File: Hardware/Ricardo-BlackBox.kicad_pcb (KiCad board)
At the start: 4 copper layers, 45.1 x 35.1 mm, 83 parts, among them J1 RBUS, J2 USB_C_Receptacle_USB2.0, J3 Conn_01x08_Pin, U1 ESP32-S3, U2 SN65HVD230, U3 LM66200DRLR, U4 MAX77827AEFD+T, U5 SC4215ASTRT, U7 LM66200DRLR, Y1 R940000171

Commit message: Rearranging ESP32 CLC
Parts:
- moved C5 2.61 mm to (94.6, 60.0), turned to 180 degrees
- moved C1 2.51 mm to (94.6, 59.0), turned to 180 degrees
- moved L1 2.35 mm to (96.6, 59.0), turned to 0 degrees
- moved C4 1.99 mm to (96.6, 60.0), turned to 0 degrees
- moved C6 1.67 mm to (98.1, 59.5), turned to 90 degrees
- moved C7 1.30 mm to (99.1, 57.5)
- moved C9 1.30 mm to (100.1, 57.5)
- moved C11 0.20 mm to (108.8, 57.9)
- moved R6 0.15 mm to (106.9, 57.9)
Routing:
- net +3V3: track 25.6 -> 22.1 mm
- net /CAN_RX: track 30.5 -> 31.5 mm
- net /CHIP_PU: track 29.8 -> 28.8 mm
- net /CAN_TX: track 25.9 -> 26.9 mm
- net /BOOT: track 34.6 -> 33.7 mm
- net Net-(C6-Pad1): track 4.07 -> 4.67 mm
- net GND: vias 53 -> 54
- added copper zone on F.Cu, net Net-(C6-Pad1)

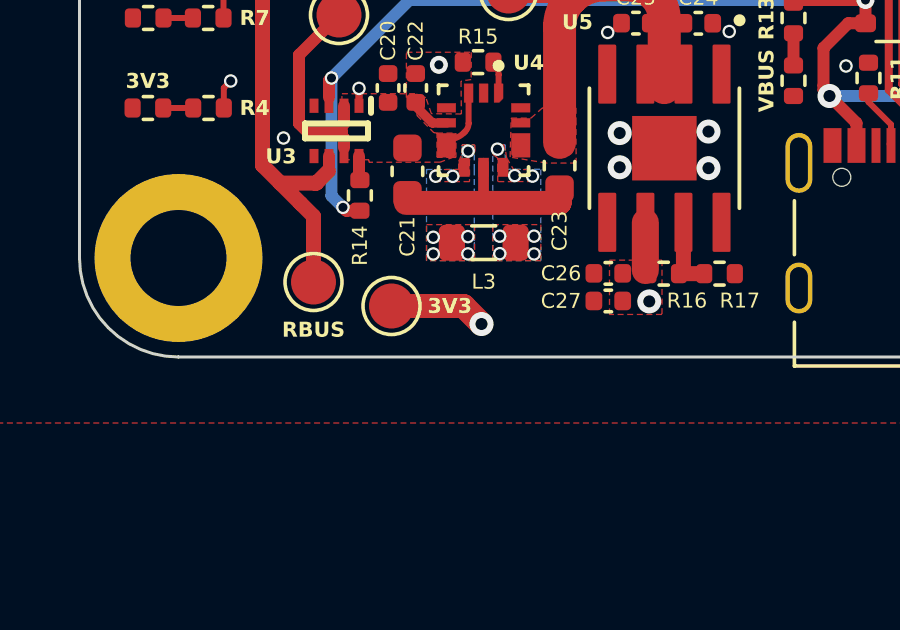
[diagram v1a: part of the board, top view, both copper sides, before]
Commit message: Fixed fill zones
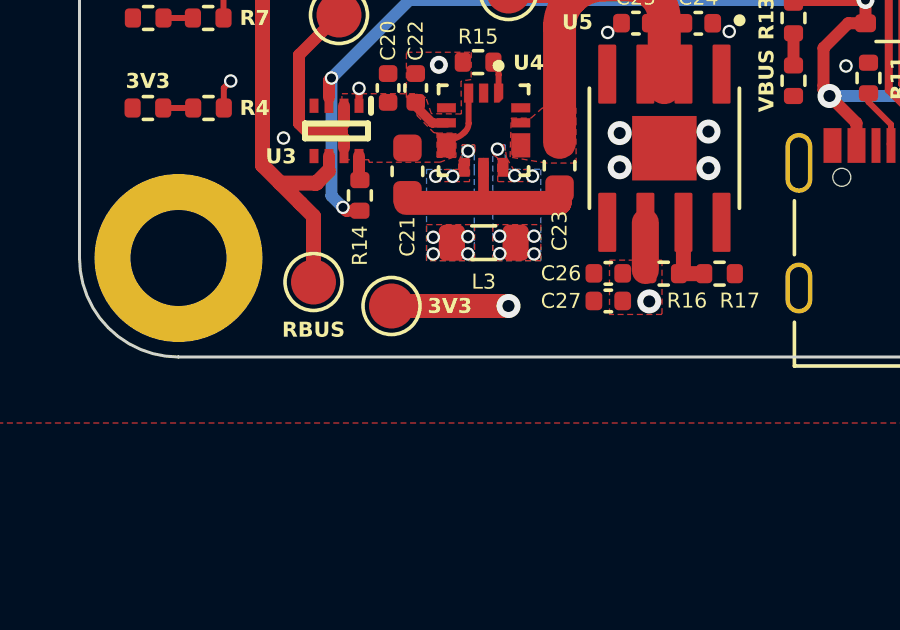
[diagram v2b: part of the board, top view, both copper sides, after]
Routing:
- net +3V3: track 22.1 -> 22.7 mm
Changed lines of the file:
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@@
 	)
 	(segment
-		(start 91.925 79.19)
-		(end 89.525 79.19)
-		(width 0.8)
-		(layer "F.Cu")
-		(net 2)
-	)
-	(segment
 		(start 113.275 70.512)
 		(end 113.275 70.94)
@@
 	)
 	(segment
-		(start 92.525 79.79)
-		(end 91.925 79.19)
+		(start 93.425 79.19)
+		(end 89.525 79.19)
 		(width 0.8)
 		(layer "F.Cu")
@@
 	)
 	(via
-		(at 92.525 79.79)
+		(at 93.425 79.19)
 		(size 0.8)
 		(drill 0.4)
@@
 	)
 	(zone
-		(net 3)
-		(net_name "VBUS")
-		(layer "F.Cu")
-		(name "$teardrop_padvia$")
-		(hatch full 0.1)
-		(priority 30000)
-		(attr
-			(teardrop
-				(type padvia)
-			)
-		)
-		(connect_pads yes
-			(clearance 0)
-		)
-		(min_thickness 0.0254)
-		(filled_areas_thickness no)
-		(fill yes
-			(thermal_gap 0.5)
-			(thermal_bridge_width 0.5)
-			(island_removal_mode 1)
-			(island_area_min 10)
-		)
-		(polygon
-			(pts
-				(xy 88.322458 76.213882) (xy 88.322458 75.813882) (xy 87.992992 75.694009) (xy 87.905888 75.901882)
-				(xy 87.820784 76.109755)
-			)
-		)
-	)
-	(zone
 		(net 7)
 		(net_name "/Power/BBOUT")
@@
 	)
 	(zone
+		(net 3)
+		(net_name "VBUS")
+		(layer "F.Cu")
+		(name "$teardrop_padvia$")
+		(hatch full 0.1)
+		(priority 30000)
+		(attr
+			(teardrop
+				(type padvia)
+			)
+		)
+		(connect_pads yes
+			(clearance 0)
+		)
+		(min_thickness 0.0254)
+		(filled_areas_thickness no)
+		(fill yes
+			(thermal_gap 0.5)
+			(thermal_bridge_width 0.5)
+			(island_removal_mode 1)
+			(island_area_min 10)
+		)
+		(polygon
+			(pts
+				(xy 88.322458 76.213882) (xy 88.322458 75.813882) (xy 87.992992 75.694009) (xy 87.905888 75.901882)
+				(xy 87.820784 76.109755)
+			)
+		)
+	)
+	(zone
 		(net 2)
 		(net_name "+3V3")
@@
 		(hatch edge 0.508)
 		(priority 5)
-		(connect_pads
+		(connect_pads yes
 			(clearance 0)
 		)
@@
 	)
 	(zone
+		(net 1)
+		(net_name "GND")
+		(layer "F.Cu")
+		(name "$teardrop_padvia$")
+		(hatch full 0.1)
+		(priority 30002)
+		(attr
+			(teardrop
+				(type padvia)
+			)
+		)
+		(connect_pads yes
+			(clearance 0)
+		)
+		(min_thickness 0.0254)
+		(filled_areas_thickness no)
+		(fill yes
+			(thermal_gap 0.5)
+			(thermal_bridge_width 0.5)
+			(island_removal_mode 1)
+			(island_area_min 10)
+		)
+		(polygon
+			(pts
+				(xy 88.316888 72.386882) (xy 88.566888 72.386882) (xy 88.649761 72.022986) (xy 88.441888 71.935882)
+				(xy 88.234015 72.022986)
+			)
+		)
+	)
+	(zone
 		(net 76)
 		(net_name "Net-(C6-Pad1)")
@@
 		(layer "F.Cu")
 		(hatch edge 0.5)
-		(priority 1)
 		(connect_pads yes
 			(clearance 0)
@@
 	)
 	(zone
-		(net 1)
-		(net_name "GND")
+		(net 3)
+		(net_name "VBUS")
 		(layer "F.Cu")
 		(name "$teardrop_padvia$")
 		(hatch full 0.1)
-		(priority 30002)
+		(priority 30001)
 		(attr
 			(teardrop
@@
 		(polygon
 			(pts
-				(xy 88.316888 72.386882) (xy 88.566888 72.386882) (xy 88.649761 72.022986) (xy 88.441888 71.935882)
-				(xy 88.234015 72.022986)
+				(xy 87.241888 72.023468) (xy 87.641888 72.023468) (xy 87.732873 71.676104) (xy 87.525 71.589) (xy 87.3 71.59)
 			)
 		)
@@
 	)
 	(zone
-		(net 3)
-		(net_name "VBUS")
-		(layer "F.Cu")
-		(name "$teardrop_padvia$")
-		(hatch full 0.1)
-		(priority 30001)
-		(attr
-			(teardrop
-				(type padvia)
-			)
-		)
-		(connect_pads yes
-			(clearance 0)
-		)
-		(min_thickness 0.0254)
-		(filled_areas_thickness no)
-		(fill yes
-			(thermal_gap 0.5)
-			(thermal_bridge_width 0.5)
-			(island_removal_mode 1)
-			(island_area_min 10)
-		)
-		(polygon
-			(pts
-				(xy 87.241888 72.023468) (xy 87.641888 72.023468) (xy 87.732873 71.676104) (xy 87.525 71.589) (xy 87.3 71.59)
-			)
-		)
-	)
-	(zone
 		(net 0)
 		(net_name "")
@@
 	)
 	(zone
+		(net 3)
+		(net_name "VBUS")
+		(layer "B.Cu")
+		(name "$teardrop_padvia$")
+		(hatch full 0.1)
+		(priority 30002)
+		(attr
+			(teardrop
+				(type padvia)
+			)
+		)
+		(connect_pads yes
+			(clearance 0)
+		)
+		(min_thickness 0.0254)
+		(filled_areas_thickness no)
+		(fill yes
+			(thermal_gap 0.5)
+			(thermal_bridge_width 0.5)
+			(island_removal_mode 1)
+			(island_area_min 10)
+		)
+		(polygon
+			(pts
+				(xy 87.730112 75.442263) (xy 87.447269 75.725106) (xy 87.747789 76.060981) (xy 87.907595 75.902589)
+				(xy 88.065987 75.742783)
+			)
+		)
+	)
+	(zone
+		(net 3)
+		(net_name "VBUS")
+		(layer "B.Cu")
+		(name "$teardrop_padvia$")
+		(hatch full 0.1)
+		(priority 30000)
+		(attr
+			(teardrop
+				(type padvia)
+			)
+		)
+		(connect_pads yes
+			(clearance 0)
+		)
+		(min_thickness 0.0254)
+		(filled_areas_thickness no)
+		(fill yes
+			(thermal_gap 0.5)
+			(thermal_bridge_width 0.5)
+			(island_removal_mode 1)
+			(island_area_min 10)
+		)
+		(polygon
+			(pts
+				(xy 87.325 72.04) (xy 87.725 72.04) (xy 87.75 71.59) (xy 87.525 71.589) (xy 87.3 71.59)
+			)
+		)
+	)
+	(zone
 		(net 9)
 		(net_name "/Power/LX2")
@@
 		(name "$teardrop_padvia$")
 		(hatch full 0.1)
-		(priority 30002)
+		(priority 30001)
 		(attr
 			(teardrop
@@
 		(polygon
 			(pts
-				(xy 87.730112 75.442263) (xy 87.447269 75.725106) (xy 87.747789 76.060981) (xy 87.907595 75.902589)
-				(xy 88.065987 75.742783)
+				(xy 87.984619 71.413224) (xy 87.701776 71.130381) (xy 87.365901 71.430901) (xy 87.524293 71.590707)
+				(xy 87.684099 71.749099)
 			)
 		)
@@
 			)
 		)
-	)
-	(zone
-		(net 3)
-		(net_name "VBUS")
-		(layer "B.Cu")
-		(name "$teardrop_padvia$")
-		(hatch full 0.1)
-		(priority 30000)
-		(attr
-			(teardrop
-				(type padvia)
-			)
-		)
-		(connect_pads yes
-			(clearance 0)
-		)
-		(min_thickness 0.0254)
-		(filled_areas_thickness no)
-		(fill yes
-			(thermal_gap 0.5)
-			(thermal_bridge_width 0.5)
-			(island_removal_mode 1)
-			(island_area_min 10)
-		)
-		(polygon
-			(pts
-				(xy 87.325 72.04) (xy 87.725 72.04) (xy 87.75 71.59) (xy 87.525 71.589) (xy 87.3 71.59)
-			)
-		)
-	)
-	(zone
-		(net 3)
-		(net_name "VBUS")
-		(layer "B.Cu")
-		(name "$teardrop_padvia$")
-		(hatch full 0.1)
-		(priority 30001)
-		(attr
-			(teardrop
-				(type padvia)
-			)
-		)
-		(connect_pads yes
-			(clearance 0)
-		)
-		(min_thickness 0.0254)
-		(filled_areas_thickness no)
-		(fill yes
-			(thermal_gap 0.5)
-			(thermal_bridge_width 0.5)
-			(island_removal_mode 1)
-			(island_area_min 10)
-		)
-		(polygon
-			(pts
-				(xy 87.984619 71.413224) (xy 87.701776 71.130381) (xy 87.365901 71.430901) (xy 87.524293 71.590707)
-				(xy 87.684099 71.749099)
-			)
-		)

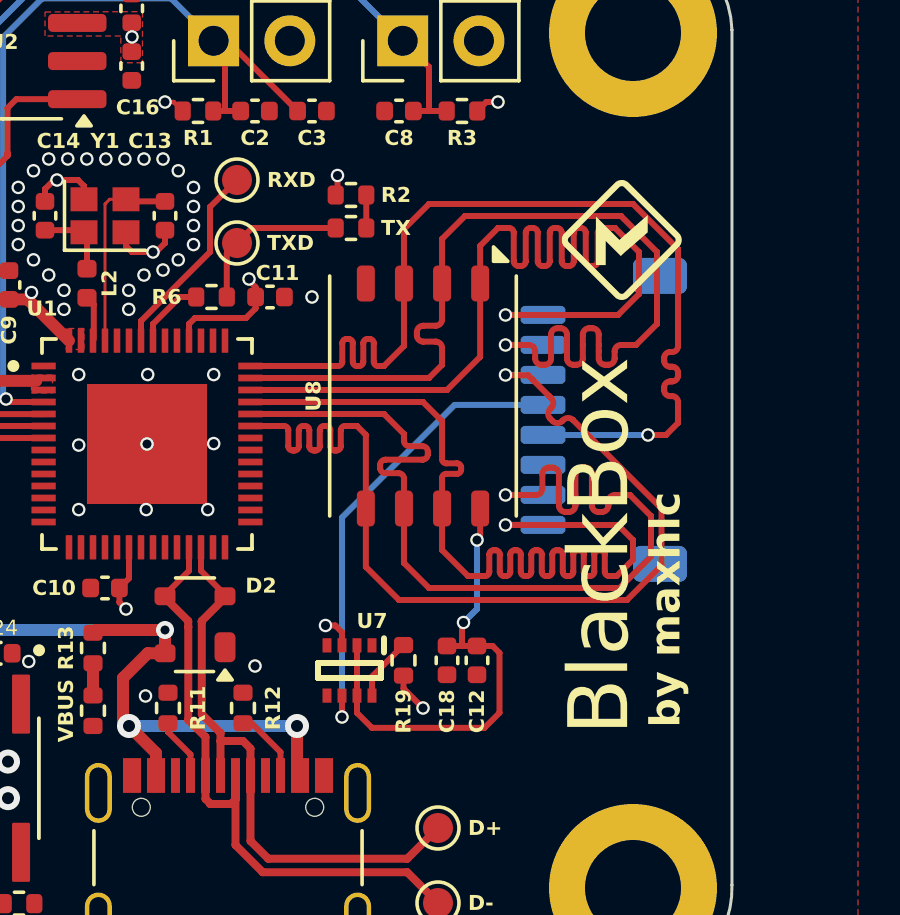
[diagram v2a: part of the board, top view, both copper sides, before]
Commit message: Moved NAND flash chip and added debounce resistor
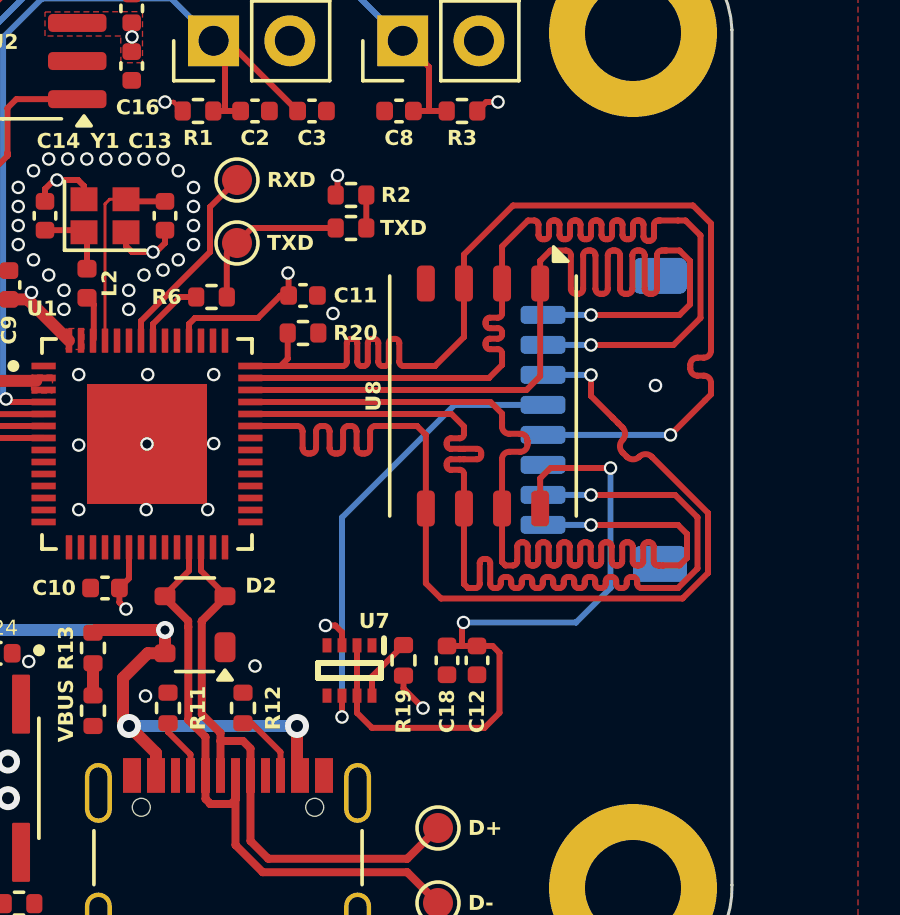
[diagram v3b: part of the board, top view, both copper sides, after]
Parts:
- removed G***: LOGO, iclr:rae_logo_4mm
- added R20: R, Resistor_SMD:R_0402_1005Metric, F.Cu at (109.9, 59.1)
- moved U8 2.00 mm to (115.9, 61.2)
- moved C11 1.10 mm to (109.9, 57.8)
- renumbered TX to TXD
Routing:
- net /NAND_3V3: track 16.1 -> 24.9 mm
- net /NAND_CLK: track 34.0 -> 38.1 mm
- net /NAND_SD2: track 34.0 -> 35.8 mm
- net /NAND_CMD: track 34.0 -> 35.8 mm
- net /NAND_SD1: track 34.0 -> 35.8 mm
- net /NAND_SD3: track 34.0 -> 35.8 mm
- net /NAND_SD0: track 34.0 -> 35.7 mm
- net +3V3: track 22.7 -> 23.7 mm
- net GND: vias 54 -> 55
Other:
- board text removed: "BlackBox"
- board text removed: "by maxhlc"

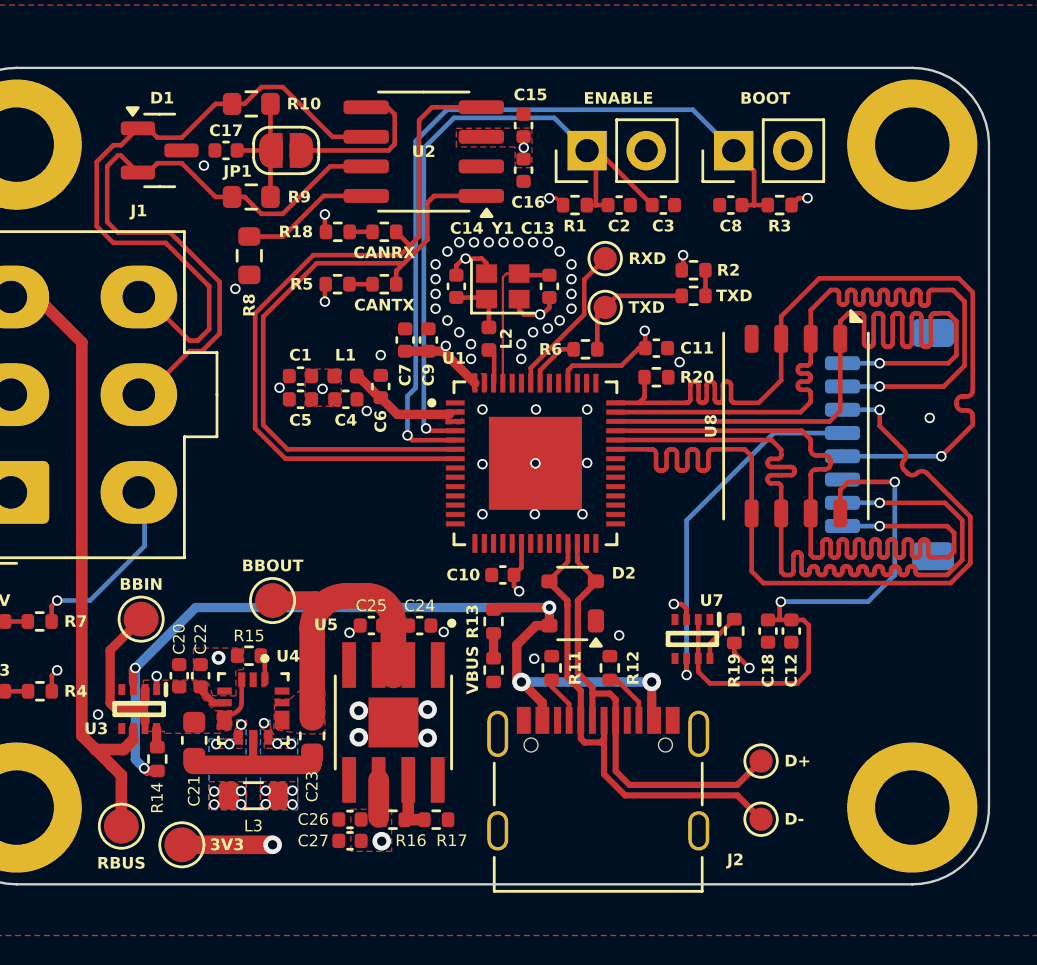
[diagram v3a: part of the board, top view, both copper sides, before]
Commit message: Rearranged NAND 3V3 switching and fixed buck-boost overlaps
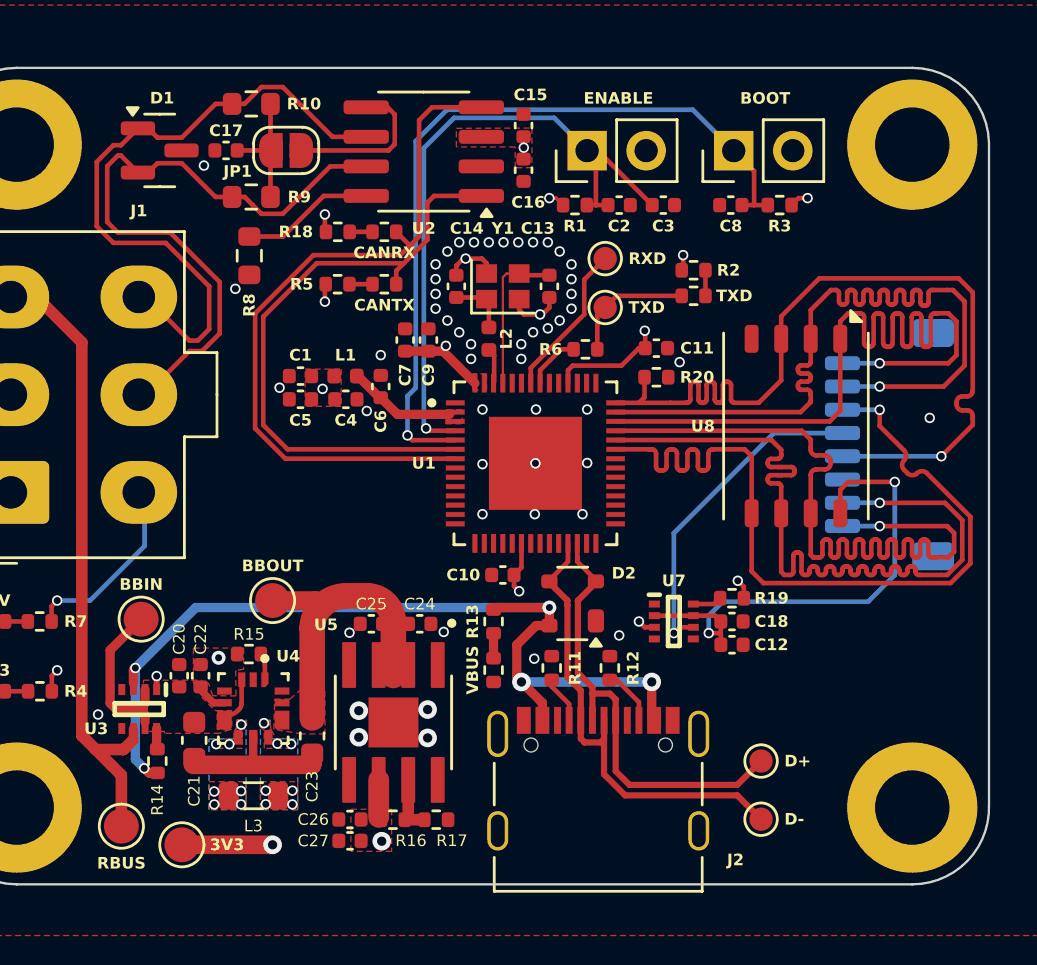
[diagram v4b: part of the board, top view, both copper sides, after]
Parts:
- moved C12 2.62 mm to (113.2, 70.6), turned to 0 degrees
- moved C18 1.60 mm to (113.2, 69.6), turned to 0 degrees
- moved R19 1.42 mm to (113.2, 68.6), turned to 0 degrees
- moved U7 1.10 mm to (110.7, 69.6), turned to 0 degrees
- moved R14 0.09 mm to (88.5, 75.6)
- moved C24 0.08 mm to (99.8, 69.7)
- moved C25 0.07 mm to (97.7, 69.7)
- moved R15 0.07 mm to (92.4, 71.0)
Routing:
- net /NAND_3V3: track 24.9 -> 21.4 mm
- net /HEADER_3V3: track 15.6 -> 14.3 mm
- net Net-(U7-ST): track 2.12 -> 1.26 mm
- net +3V3: track 23.7 -> 22.9 mm

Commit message: Hoisted the colours
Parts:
- added G***: LOGO, iclr:iclr_logo_estd2018_6mm, F.Cu at (119.5, 71.3)
- added G***: LOGO, iclr:iclr_logo_estd2018_6mm, B.Cu at (89.9, 76.1)
- added G***: LOGO, iclr:rae_logo_6mm, B.Cu at (96.9, 76.1)
- added REF**: jolly_roger, iclr:jolly_roger, B.Cu at (103.2, 62.5)
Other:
- board text added: "Designed by Max Hallgarten La Casta Electronics 2025"
- board text added: "JOLLY ROGER v1.0"
